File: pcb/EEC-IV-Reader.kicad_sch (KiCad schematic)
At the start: 32 parts, among them J1 ARDUINO_1, J2 ARDUINO_2, J3 RS_485_DEBUG, J4 ARDUINO_3, J5 ARDUINO_4, J6 DISPLAY, J7 OBD, J8 I2C_DEBUG, J9 Vin_disconnect, SW1 BTN_UP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

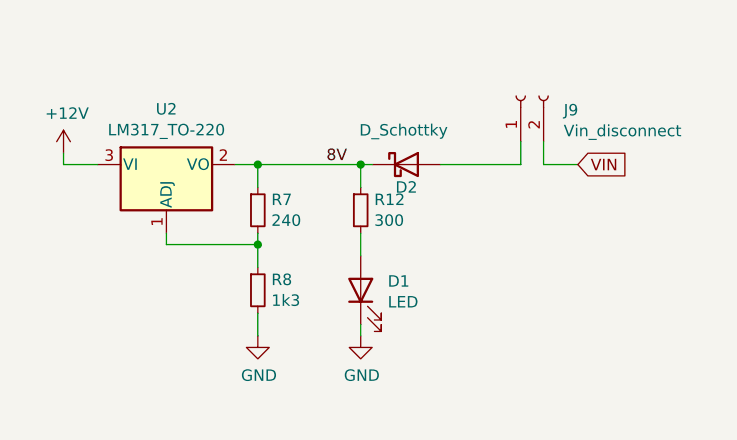
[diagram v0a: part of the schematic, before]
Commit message: Update LED Labels and Diode direction
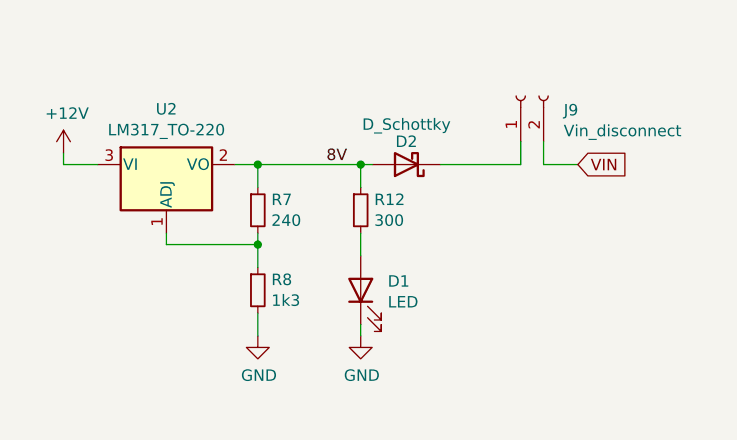
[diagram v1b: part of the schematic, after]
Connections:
- net 8V: now also D2.2 (A); no longer D2.1 (K)
- net at J9.1 (Pin_1): now also D2.1 (K); no longer D2.2 (A)
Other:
- moved on the sheet: D2
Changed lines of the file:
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@@
     (pin "2")
   )
-  (symbol (lib_id "Device:D_Schottky") (at 242.57 29.21 0) (unit 1)
+  (symbol (lib_id "Device:D_Schottky") (at 242.57 29.21 180) (unit 1)
     (in_bom yes) (on_board yes)
-    (property "Reference" "D2" (id 0) (at 242.57 31.75 0))
-    (property "Value" "D_Schottky" (id 1) (at 242.2525 25.4 0))
+    (property "Reference" "D2" (id 0) (at 242.57 26.67 0))
+    (property "Value" "D_Schottky" (id 1) (at 242.57 24.765 0))
     (property "Footprint" "Diode_THT:D_A-405_P7.62mm_Horizontal" (id 2) (at 242.57 29.21 0)
       (effects (font (size 1.27 1.27)) hide)

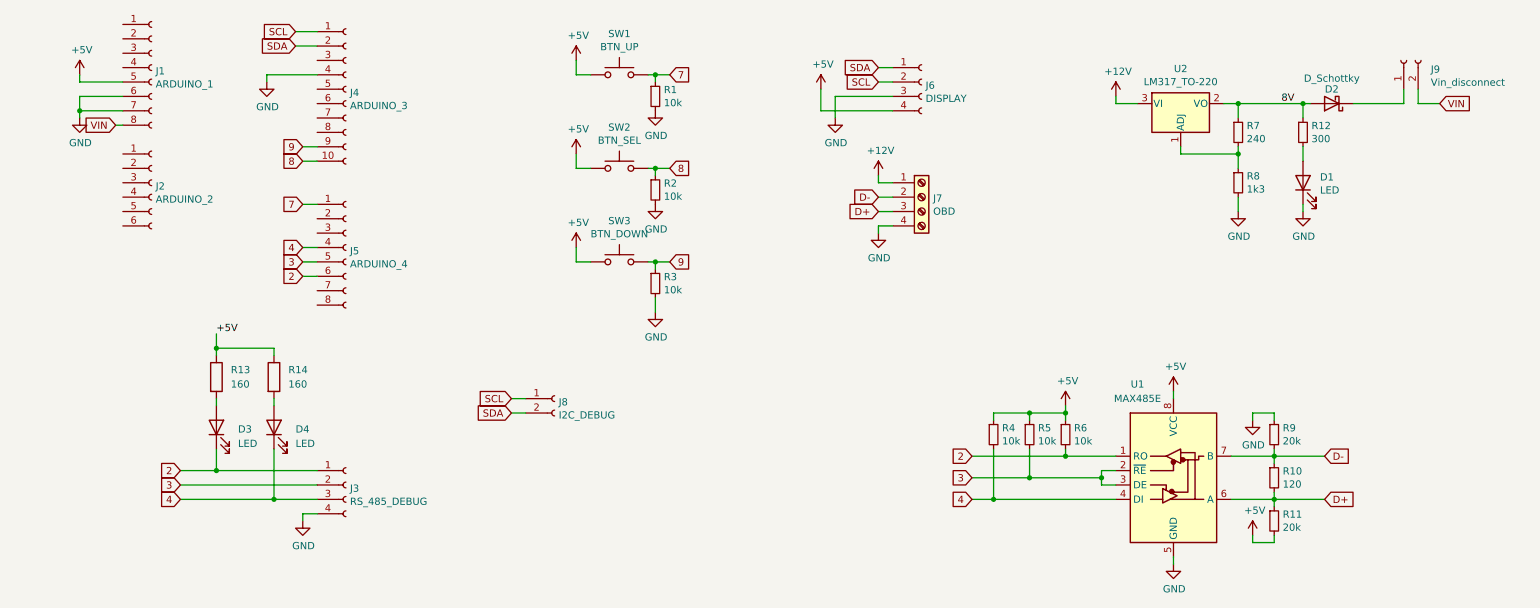
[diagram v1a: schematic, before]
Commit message: Add voltage divider to measure battery voltage
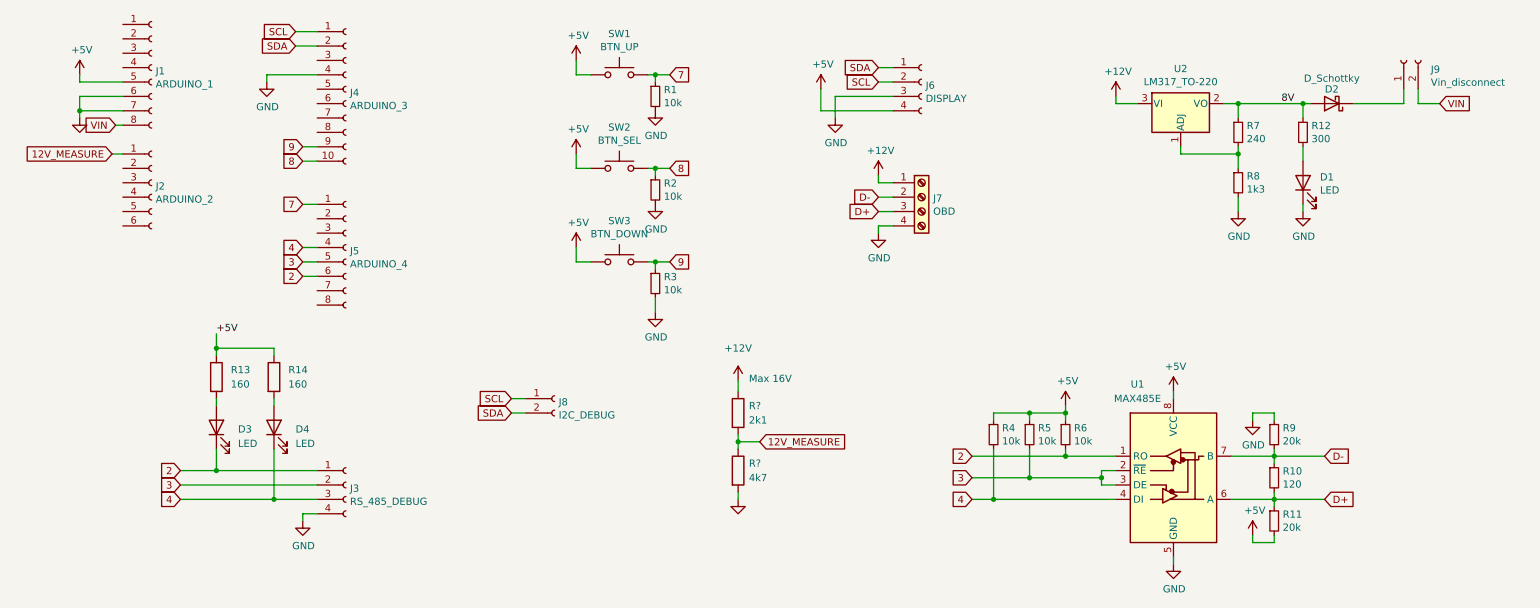
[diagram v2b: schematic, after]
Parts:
- added R?: 4k7, Resistor_THT:R_Axial_DIN0207_L6.3mm_D2.5mm_P7.62mm_Horizontal, symbol Device:R
- added R?: 2k1, Resistor_THT:R_Axial_DIN0207_L6.3mm_D2.5mm_P7.62mm_Horizontal, symbol Device:R
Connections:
- net +12V: now also R?.1
- net GND: now also R?.2
- net 12V_MEASURE: now reaches J2.1 (Pin_1)
- net 12V_MEASURE: now also R?.1, R?.2
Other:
- note added: "Max 16V"
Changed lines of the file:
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@@
   (junction (at 182.88 99.06) (diameter 0) (color 0 0 0 0)
   )
+  (junction (at 137.795 88.9) (diameter 0) (color 0 0 0 0)
+  )
   (junction (at 123.19 24.13) (diameter 0) (color 0 0 0 0)
   )
@@
     (stroke (width 0) (type default) (color 0 0 0 0))
   )
+  (wire (pts (xy 27.305 38.1) (xy 29.21 38.1))
+    (stroke (width 0) (type default) (color 0 0 0 0))
+  )
   (wire (pts (xy 226.06 29.21) (xy 226.06 31.75))
     (stroke (width 0) (type default) (color 0 0 0 0))
@@
     (stroke (width 0) (type default) (color 0 0 0 0))
   )
+  (wire (pts (xy 137.795 78.105) (xy 137.795 80.01))
+    (stroke (width 0) (type default) (color 0 0 0 0))
+  )
   (wire (pts (xy 39.37 93.98) (xy 45.72 93.98))
     (stroke (width 0) (type default) (color 0 0 0 0))
@@
     (stroke (width 0) (type default) (color 0 0 0 0))
   )
+  (wire (pts (xy 137.795 97.79) (xy 137.795 99.06))
+    (stroke (width 0) (type default) (color 0 0 0 0))
+  )
   (wire (pts (xy 123.19 63.5) (xy 123.19 66.04))
     (stroke (width 0) (type default) (color 0 0 0 0))
@@
     (stroke (width 0) (type default) (color 0 0 0 0))
   )
+  (wire (pts (xy 137.795 88.9) (xy 137.795 90.17))
+    (stroke (width 0) (type default) (color 0 0 0 0))
+  )
   (wire (pts (xy 123.19 40.64) (xy 125.73 40.64))
     (stroke (width 0) (type default) (color 0 0 0 0))
@@
     (stroke (width 0) (type default) (color 0 0 0 0))
   )
+  (wire (pts (xy 137.795 87.63) (xy 137.795 88.9))
+    (stroke (width 0) (type default) (color 0 0 0 0))
+  )
   (wire (pts (xy 195.58 83.82) (xy 195.58 85.09))
     (stroke (width 0) (type default) (color 0 0 0 0))
@@
     (stroke (width 0) (type default) (color 0 0 0 0))
   )
+  (wire (pts (xy 137.795 88.9) (xy 141.605 88.9))
+    (stroke (width 0) (type default) (color 0 0 0 0))
+  )
   (wire (pts (xy 195.58 91.44) (xy 195.58 90.17))
     (stroke (width 0) (type default) (color 0 0 0 0))
@@
   (wire (pts (xy 109.22 57.15) (xy 111.76 57.15))
     (stroke (width 0) (type default) (color 0 0 0 0))
+  )
+  (text "Max 16V" (at 139.7 78.74 0)
+    (effects (font (size 1.27 1.27)) (justify left bottom))
   )
   (label "+5V" (at 45.72 69.85 0)
@@
     )
   )
+  (global_label "12V_MEASURE" (shape input) (at 141.605 88.9 0) (fields_autoplaced)
+    (effects (font (size 1.27 1.27)) (justify left))
+    (property "Intersheet References" "${INTERSHEET_REFS}" (id 0) (at 157.0525 88.8206 0)
+      (effects (font (size 1.27 1.27)) (justify left) hide)
+    )
+  )
   (global_label "9" (shape input) (at 60.96 36.83 180) (fields_autoplaced)
     (effects (font (size 1.27 1.27)) (justify right))
@@
     (property "Intersheet References" "${INTERSHEET_REFS}" (id 0) (at 0 0 0)
       (effects (font (size 1.27 1.27)) hide)
+    )
+  )
+  (global_label "12V_MEASURE" (shape input) (at 27.305 38.1 180) (fields_autoplaced)
+    (effects (font (size 1.27 1.27)) (justify right))
+    (property "Intersheet References" "${INTERSHEET_REFS}" (id 0) (at 11.8575 38.0206 0)
+      (effects (font (size 1.27 1.27)) (justify right) hide)
     )
   )
@@
       (effects (font (size 1.27 1.27)) hide)
     )
-    (property "Value" "GND" (id 1) (at 21.717 36.1442 0))
+    (property "Value" "GND" (id 1) (at 21.717 36.1442 0)
+      (effects (font (size 1.27 1.27)) hide)
+    )
     (property "Footprint" "" (id 2) (at 21.59 31.75 0)
       (effects (font (size 1.27 1.27)) hide)
@@
     (pin "2")
   )
+  (symbol (lib_id "Device:R") (at 137.795 93.98 0) (unit 1)
+    (in_bom yes) (on_board yes) (fields_autoplaced)
+    (property "Reference" "R?" (id 0) (at 139.7 92.7099 0)
+      (effects (font (size 1.27 1.27)) (justify left))
+    )
+    (property "Value" "4k7" (id 1) (at 139.7 95.2499 0)
+      (effects (font (size 1.27 1.27)) (justify left))
+    )
+    (property "Footprint" "Resistor_THT:R_Axial_DIN0207_L6.3mm_D2.5mm_P7.62mm_Horizontal" (id 2) (at 136.017 93.98 90)
+      (effects (font (size 1.27 1.27)) hide)
+    )
+    (property "Datasheet" "~" (id 3) (at 137.795 93.98 0)
+      (effects (font (size 1.27 1.27)) hide)
+    )
+    (pin "1")
+    (pin "2")
+  )
+  (symbol (lib_id "Device:R") (at 137.795 83.82 0) (unit 1)
+    (in_bom yes) (on_board yes) (fields_autoplaced)
+    (property "Reference" "R?" (id 0) (at 139.7 82.5499 0)
+      (effects (font (size 1.27 1.27)) (justify left))
+    )
+    (property "Value" "2k1" (id 1) (at 139.7 85.0899 0)
+      (effects (font (size 1.27 1.27)) (justify left))
+    )
+    (property "Footprint" "Resistor_THT:R_Axial_DIN0207_L6.3mm_D2.5mm_P7.62mm_Horizontal" (id 2) (at 136.017 83.82 90)
+      (effects (font (size 1.27 1.27)) hide)
+    )
+    (property "Datasheet" "~" (id 3) (at 137.795 83.82 0)
+      (effects (font (size 1.27 1.27)) hide)
+    )
+    (pin "1")
+    (pin "2")
+  )
+  (symbol (lib_id "power:+12V") (at 137.795 78.105 0) (unit 1)
+    (in_bom yes) (on_board yes) (fields_autoplaced)
+    (property "Reference" "#PWR?" (id 0) (at 137.795 81.915 0)
+      (effects (font (size 1.27 1.27)) hide)
+    )
+    (property "Value" "+12V" (id 1) (at 137.795 72.39 0))
+    (property "Footprint" "" (id 2) (at 137.795 78.105 0)
+      (effects (font (size 1.27 1.27)) hide)
+    )
+    (property "Datasheet" "" (id 3) (at 137.795 78.105 0)
+      (effects (font (size 1.27 1.27)) hide)
+    )
+    (pin "1")
+  )
   (symbol (lib_id "Device:D_Schottky") (at 242.57 29.21 180) (unit 1)
     (in_bom yes) (on_board yes)
@@
     (pin "1")
     (pin "2")
+  )
+  (symbol (lib_name "GND_1") (lib_id "power:GND") (at 137.795 99.06 0) (unit 1)
+    (in_bom yes) (on_board yes) (fields_autoplaced)
+    (property "Reference" "#PWR?" (id 0) (at 137.795 105.41 0)
+      (effects (font (size 1.27 1.27)) hide)
+    )
+    (property "Value" "GND" (id 1) (at 137.795 104.14 0)
+      (effects (font (size 1.27 1.27)) hide)
+    )
+    (property "Footprint" "" (id 2) (at 137.795 99.06 0)
+      (effects (font (size 1.27 1.27)) hide)
+    )
+    (property "Datasheet" "" (id 3) (at 137.795 99.06 0)
+      (effects (font (size 1.27 1.27)) hide)
+    )
+    (pin "1")
   )
   (symbol (lib_id "Device:R") (at 55.88 77.47 0) (unit 1)
@@
       (reference "#PWR022") (unit 1) (value "GND") (footprint "")
     )
+    (path "/2ee17aa1-bafd-4c7c-a1f7-9a9fc823fd2a"
+      (reference "#PWR?") (unit 1) (value "+12V") (footprint "")
+    )
+    (path "/bba240c3-f486-4079-903b-9a48b8320704"
+      (reference "#PWR?") (unit 1) (value "GND") (footprint "")
+    )
     (path "/00000000-0000-0000-0000-00006250e0f7"
       (reference "D1") (unit 1) (value "LED") (footprint "LED_THT:LED_D3.0mm")
@@
       (reference "R14") (unit 1) (value "160") (footprint "Resistor_THT:R_Axial_DIN0207_L6.3mm_D2.5mm_P7.62mm_Horizontal")
     )
+    (path "/0f97ec3b-8224-4a57-aeb5-ca1144a139ad"
+      (reference "R?") (unit 1) (value "4k7") (footprint "Resistor_THT:R_Axial_DIN0207_L6.3mm_D2.5mm_P7.62mm_Horizontal")
+    )
+    (path "/28522c6a-4bdf-4beb-8332-a8473ca70f3d"
+      (reference "R?") (unit 1) (value "2k1") (footprint "Resistor_THT:R_Axial_DIN0207_L6.3mm_D2.5mm_P7.62mm_Horizontal")
+    )
     (path "/00000000-0000-0000-0000-0000624fafbd"

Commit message: Fix resistor value
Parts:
- R?: value 2k1 -> 21k
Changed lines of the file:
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@@
       (effects (font (size 1.27 1.27)) (justify left))
     )
-    (property "Value" "2k1" (id 1) (at 139.7 85.0899 0)
+    (property "Value" "21k" (id 1) (at 139.7 85.0899 0)
       (effects (font (size 1.27 1.27)) (justify left))
     )
@@
     )
     (path "/28522c6a-4bdf-4beb-8332-a8473ca70f3d"
-      (reference "R?") (unit 1) (value "2k1") (footprint "Resistor_THT:R_Axial_DIN0207_L6.3mm_D2.5mm_P7.62mm_Horizontal")
+      (reference "R?") (unit 1) (value "21k") (footprint "Resistor_THT:R_Axial_DIN0207_L6.3mm_D2.5mm_P7.62mm_Horizontal")
     )
     (path "/00000000-0000-0000-0000-0000624fafbd"
